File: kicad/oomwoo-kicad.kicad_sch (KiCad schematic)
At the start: 0 parts

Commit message: Battery charging
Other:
- added sheet BATTERY-CHARGER (Battery-Charger.kicad_sch)
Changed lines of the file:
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@@
+	)
+	(sheet
+		(at 44.45 346.71)
+		(size 40.64 25.4)
+		(exclude_from_sim no)
+		(in_bom yes)
+		(on_board yes)
+		(dnp no)
+		(fields_autoplaced yes)
+		(stroke
+			(width 0.1524)
+			(type solid)
+		)
+		(fill
+			(color 0 0 0 0)
+		)
+		(property "Sheetname" "BATTERY-CHARGER"
+			(at 44.45 345.9984 0)
+			(show_name no)
+			(do_not_autoplace no)
+			(effects
+				(font
+					(size 1.27 1.27)
+				)
+				(justify left bottom)
+			)
+		)
+		(property "Sheetfile" "Battery-Charger.kicad_sch"
+			(at 44.45 372.6946 0)
+			(show_name no)
+			(do_not_autoplace no)
+			(effects
+				(font
+					(size 1.27 1.27)
+				)
+				(justify left top)
+			)
+		)
+		(instances
+			(project "oomwoo-kicad"
+				(path "/dbcfb655-8d45-4808-9a74-2a0eb03372e8"
+					(page "34")
+				)
+			)
+		)
 	)
 	(sheet

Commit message: Added Pi CM4/CM5
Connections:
- no-connect marks 4 -> 5
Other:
- removed sheet RK3562
- removed sheet WIFI-BT
- added sheet CM5-GPIO (CM5-GPIO.kicad_sch)
- added sheet CM5-HIGHSPEED (CM5-Highspeed.kicad_sch)
- sheet BATTERY-CHARGER ports: added D+, D-, ID, SCL, SDA, ~{INT}; removed none
- sheet CAMERA ports: added CAM_IO, CM4_CAM0_C_N, CM4_CAM0_C_P, CM4_CAM0_D0_N, CM4_CAM0_D0_P, CM4_CAM0_D1_N, CM4_CAM0_D1_P, ID_SC, ID_SD, MIPI0_C_N, MIPI0_C_P, MIPI0_D0_N, MIPI0_D0_P, MIPI0_D1_N, MIPI0_D1_P, MIPI1_C_N, MIPI1_C_P, MIPI1_D0_N, MIPI1_D0_P, MIPI1_D1_N, MIPI1_D1_P, SCL0, SDA0; removed CAM_CLK0_OUT, CAM_PDN0_L, CAM_RST0_L, I2C4_SCL_M0, I2C4_SDA_M0, MIPI_CSI_RX0_CLK0N, MIPI_CSI_RX0_CLK0P, MIPI_CSI_RX0_D0N, MIPI_CSI_RX0_D0P, MIPI_CSI_RX0_D1N, MIPI_CSI_RX0_D1P, MIPI_CSI_RX0_D2N, MIPI_CSI_RX0_D2P, MIPI_CSI_RX0_D3N, MIPI_CSI_RX0_D3P
- sheet MAIN-FAN ports: added FG, SP; removed MAIN-FAN-S-CTRL, MAIN-FAN-S-SENSE
- sheet MCU-STM32 ports: added BAT_ID, I2C2_SCL, I2C2_SDA, PI-RESET, SUCTION-FAN-FG, SUCTION-FAN-SP, ~{CHG_INT}; removed CHARGE-STATUS, CURENT-SENSE, MAIN-FAN-S-CTRL, MAIN-FAN-S-SENSE, RK-RESET, V-CHARGE-SENSE, VBAT-SENSE
- sheet POWER ports: added none; removed CHARGE-STATUS, CURENT-SENSE, PMIC_EXT_EN, USBC_N, USBC_P, V-CHARGE-SENSE, VBAT-SENSE
- sheet SPEAKER-MIC ports: added BCLK, DIN, DOUT, LRCLK, SP_SHUTDOWN; removed AUDIO-SD, MIC1_IN, MIC2_IN, SPK_N, SPK_P
- note removed: "RK3562"
- note removed: "WF-BT-AP6256"

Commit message: Changed MCU to STM32G473VCT6
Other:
- removed sheet DOCKING-BUMBER
- sheet MAIN-BRUSH MOTOR ports: added MAIN-BRUSH-CURRENT-ADC, MAIN-BRUSH-IN1, MAIN-BRUSH-IN2; removed MAIN-BRUSH, MAIN-BRUSH-F-ADC
- sheet MAIN-FAN ports: added MAIN-FAN-S-CTRL, MAIN-FAN-S-SENSE; removed FG, SP
- sheet MCU-STM32 ports: added I2C3_SCL, I2C3_SDA, MAIN-BRUSH-CURRENT-ADC, MAIN-BRUSH-IN1, MAIN-BRUSH-IN2, MAIN-FAN-S-CTRL, MAIN-FAN-S-SENSE, SIDE-BRUSH-CURRENT-ADC, SIDE-BRUSH-IN1, SIDE-BRUSH-IN2; removed BUMPER-SW1, BUMPER-SW2, DOC-IR-SENS1, DOC-IR-SENS2, I2C2_SCL, I2C2_SDA, MAIN-BRUSH, MAIN-BRUSH-F-ADC, SIDE-BRUSH-L-F-ADC, SIDE-BRUSH-R-F-ADC, SIDE-BRUSH-V-L-CTRL, SIDE-BRUSH-V-R-CTRL, SUCTION-FAN-FG, SUCTION-FAN-SP, WHEEL-M-EN-V
- sheet SIDE-BRUSH ports: added SIDE-BRUSH-CURRENT-ADC, SIDE-BRUSH-IN1, SIDE-BRUSH-IN2; removed SIDE-BRUSH-L-F-ADC, SIDE-BRUSH-R-F-ADC, SIDE-BRUSH-V-L-CTRL, SIDE-BRUSH-V-R-CTRL
- sheet WHEEL MOTOR ports: added none; removed WHEEL-M-EN-V
- note removed: "Controller-RK3562 CONTROLLER TOP"
- note removed: "DOC-IR BUMBER SW"

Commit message: STM32G473VCT6
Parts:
- added R1: 10, symbol Device:R_US
- added R51, R52, R53, R54, R55, R63, R65, R66, R67: 0, symbol Device:R_US
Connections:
- net CM5-GPIO/GPIO07: now also R65.1
- net IMU-CS: now also R53.1
- net IMU-FSYNC: now also R63.1
- net IMU-INT1: now also R55.1
- net IMU-INT2: now also R54.1
- net IMU-MISO: now also R52.1
- net IMU-MOSI: now also R51.1
- net IMU-SCLK: now also R1.1
- new net CM5-GPIO/GPIO22: R63.2
- new net CM5-GPIO/GPIO23: R55.2
- new net CM5-GPIO/GPIO24: R54.2
- new net CM5-GPIO/SPI0_CS0: R53.2
- new net CM5-GPIO/SPI0_MISO: R52.2
- new net CM5-GPIO/SPI0_MOSI: R51.2
- new net CM5-GPIO/SPI0_SCLK: R1.2
- new net CM5-GPIO/UART4_RX: R66.1
- new net CM5-GPIO/UART4_TX: R67.1
- new net LiDAR/LiDAR-MOTOR-CTRL: R65.2
- new net LiDAR/LiDAR-RXD: R67.2
- new net LiDAR/LiDAR-TXD: R66.2
- no-connect marks 5 -> 0
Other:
- added sheet FRONT SENSORS (Front Sensors.kicad_sch)
- added sheet M.2 (M.2.kicad_sch)
- sheet ANTI-FALL ports: added BUMPER_LED_EN, CLIFF_LED_EN; removed none
- sheet CM5-GPIO ports: added SCL1, SDA1, UART4_RX, UART4_TX; removed AUDIO_OUT_L, AUDIO_OUT_R, UART0_RX, UART0_TX
- sheet CM5-HIGHSPEED ports: added PCIE_CLK_N, PCIE_CLK_P, PCIE_CLK_nREQ, PCIE_RX_N, PCIE_RX_P, PCIE_TX_N, PCIE_TX_P, PCIE_nRST, PCIE_nWAKE; removed none
- sheet LiDAR ports: added LiDAR-TXD; removed none
- sheet MCU-STM32 ports: added BUMPER_LED_EN, CLIFF_LED_EN, STM_UART3_RX, STM_UART3_TX, USART4-IR-L-RX, USART4-IR-L-TX, USART4-IR-R-RX, USART4-IR-R-TX, WHEEL-M-LEFT-DROP, WHEEL-M-RIGHT-DROP; removed LiDAR-TXD-HEADER, STM-RESET
- sheet SPEAKER-MIC ports: added none; removed AUDIO-HP-L, AUDIO-HP-R
- sheet WHEEL MOTOR ports: added WHEEL-M-LEFT-DROP, WHEEL-M-RIGHT-DROP; removed none
- note added: "CM5-GPIOS"
- note added: "CM5-HIGHSPEED"
- note added: "FRONT SENSORS"
- note added: "M.2 CONN"

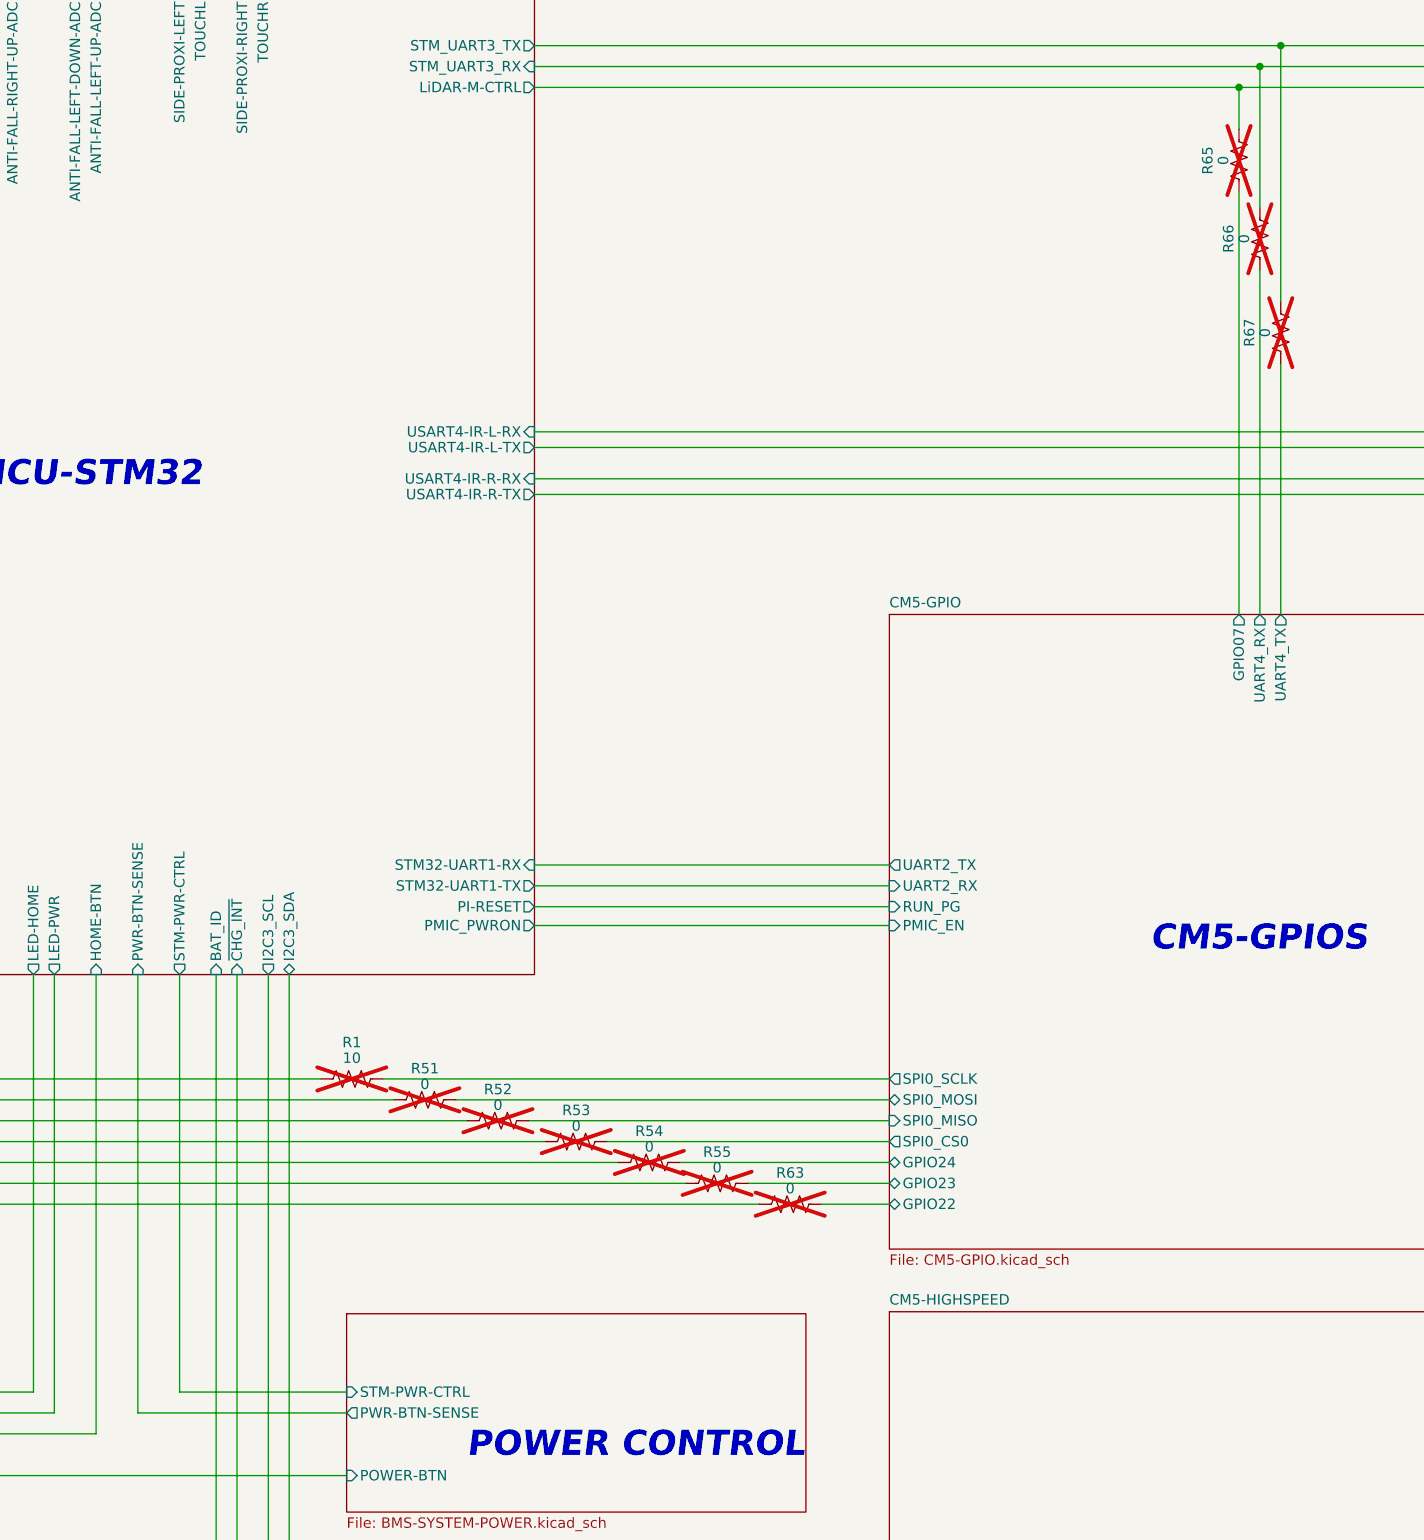
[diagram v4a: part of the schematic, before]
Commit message: RTC clock, signal integrity
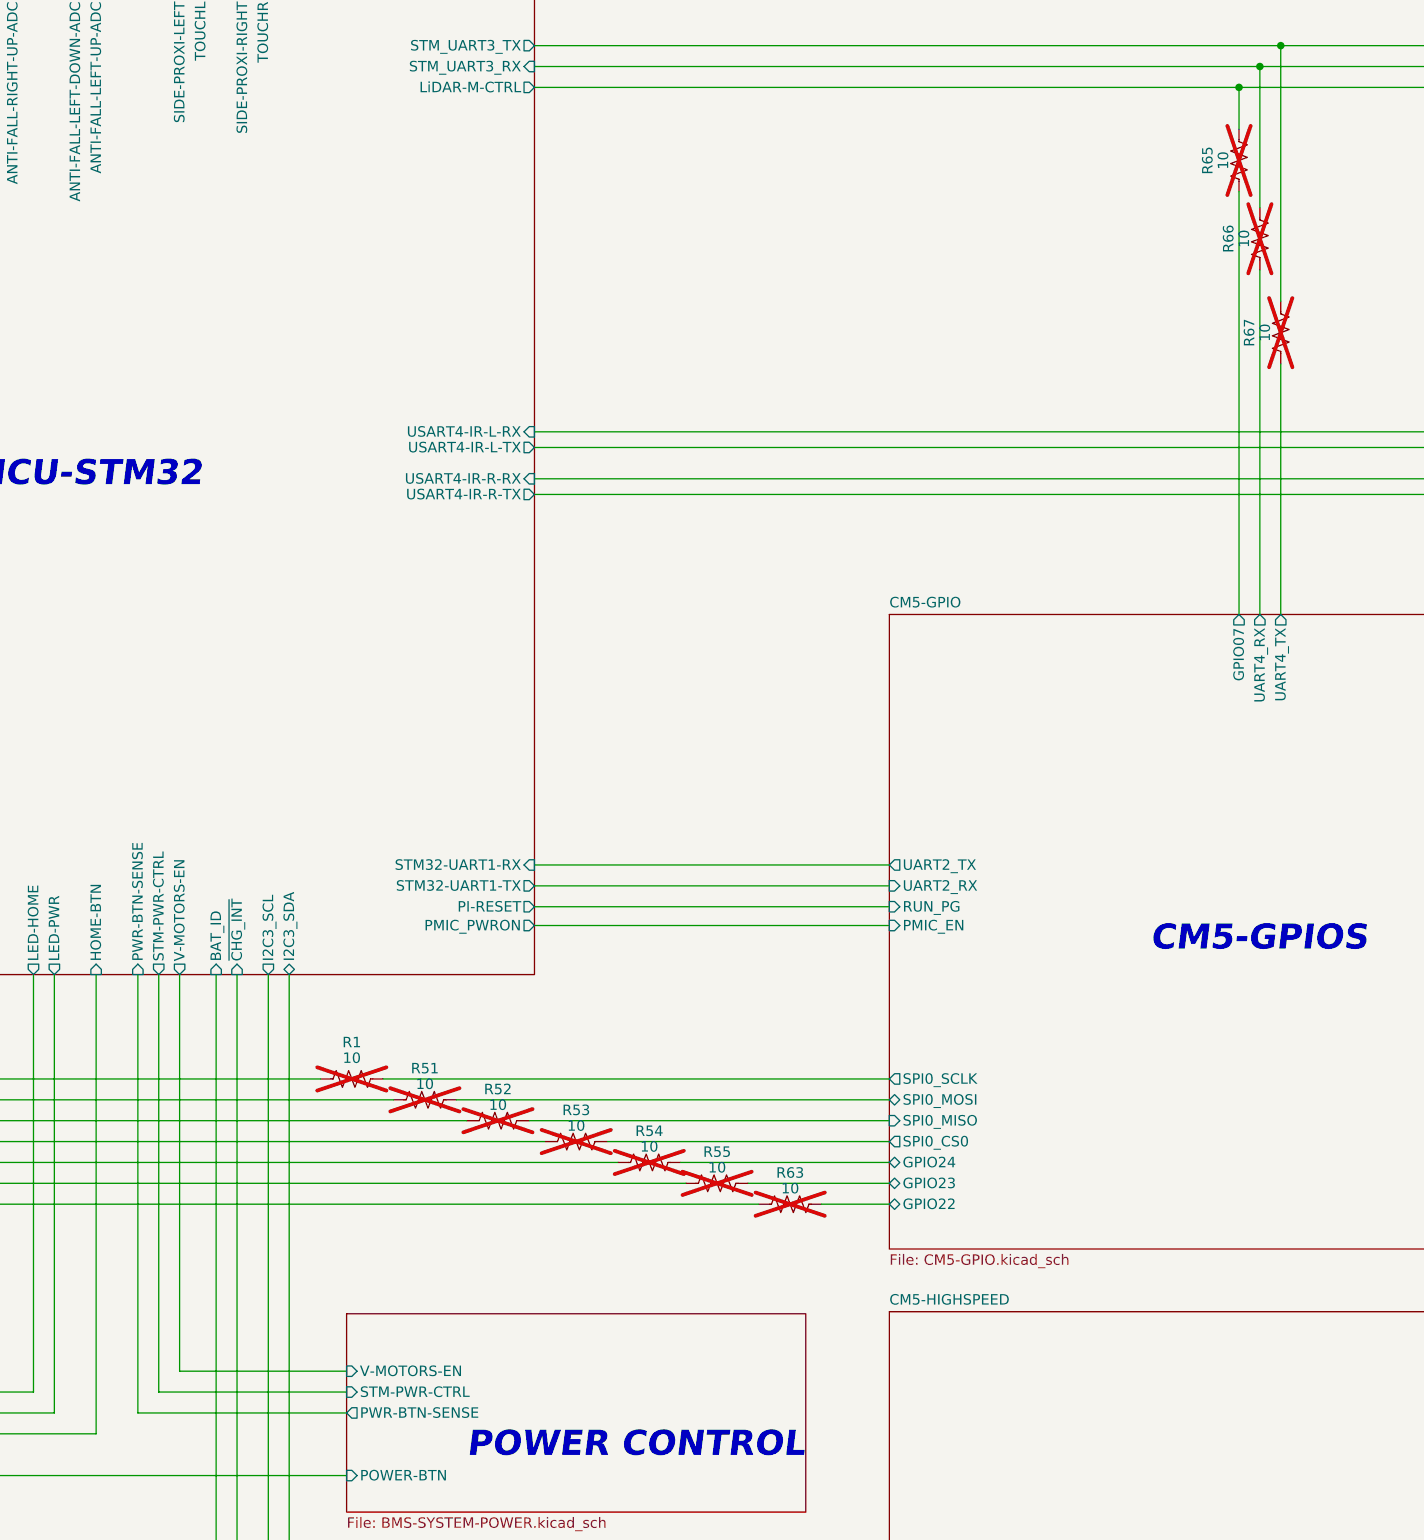
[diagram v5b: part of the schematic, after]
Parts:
- R51, R52, R53, R54, R55, R63, R65, R66, R67: value 0 -> 10
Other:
- sheet MCU-STM32 ports: added V-MOTORS-EN; removed none
- sheet POWER ports: added V-MOTORS-EN; removed none
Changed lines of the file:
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@@
 	(wire
 		(pts
+			(xy 219.71 234.315) (xy 219.71 282.575)
+		)
+		(stroke
+			(width 0)
+			(type default)
+		)
+	)
+	(wire
+		(pts
 			(xy 119.38 116.205) (xy 119.38 133.35)
 		)
@@
 	(wire
 		(pts
+			(xy 219.71 282.575) (xy 240.03 282.575)
+		)
+		(stroke
+			(width 0)
+			(type default)
+		)
+	)
+	(wire
+		(pts
 			(xy 179.07 43.18) (xy 207.01 43.18)
 		)
@@
 	(wire
 		(pts
-			(xy 240.03 285.115) (xy 219.71 285.115)
+			(xy 240.03 285.115) (xy 217.17 285.115)
 		)
 		(stroke
@@
 	(wire
 		(pts
-			(xy 219.71 285.115) (xy 219.71 234.315)
+			(xy 217.17 285.115) (xy 217.17 234.315)
 		)
 		(stroke
@@
 			)
 		)
-		(property "Value" "0"
+		(property "Value" "10"
 			(at 267.97 252.73 90)
 			(show_name no)
@@
 			)
 		)
-		(property "Value" "0"
+		(property "Value" "10"
 			(at 294.005 260.35 90)
 			(show_name no)
@@
 			)
 		)
-		(property "Value" "0"
+		(property "Value" "10"
 			(at 285.115 257.81 90)
 			(show_name no)
@@
 			)
 		)
-		(property "Value" "0"
+		(property "Value" "10"
 			(at 276.86 255.27 90)
 			(show_name no)
@@
 			)
 		)
-		(property "Value" "0"
+		(property "Value" "10"
 			(at 346.71 135.255 90)
 			(show_name no)
@@
 			)
 		)
-		(property "Value" "0"
+		(property "Value" "10"
 			(at 249.555 247.65 90)
 			(show_name no)
@@
 			)
 		)
-		(property "Value" "0"
+		(property "Value" "10"
 			(at 349.25 144.78 90)
 			(show_name no)
@@
 			)
 		)
-		(property "Value" "0"
+		(property "Value" "10"
 			(at 258.445 250.19 90)
 			(show_name no)
@@
 			)
 		)
-		(property "Value" "0"
+		(property "Value" "10"
 			(at 351.79 156.21 90)
 			(show_name no)
@@
 			)
 		)
+		(pin "V-MOTORS-EN" input
+			(at 240.03 282.575 180)
+			(effects
+				(font
+					(size 1.27 1.27)
+				)
+				(justify left)
+			)
+		)
 		(instances
 			(project "oomwoo-kicad"
@@
 		)
 		(pin "STM-PWR-CTRL" output
-			(at 219.71 234.315 270)
+			(at 217.17 234.315 270)
 			(effects
 				(font
@@
 			)
 		)
+		(pin "V-MOTORS-EN" output
+			(at 219.71 234.315 270)
+			(effects
+				(font
+					(size 1.27 1.27)
+				)
+				(justify left)
+			)
+		)

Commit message: External RTC; IR light; side sensors
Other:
- added sheet RTC_WATCHDOG (RTC_WATCHDOG.kicad_sch)
- sheet CM5-GPIO ports: added PMIC_EN2; removed none
- sheet FRONT SENSORS ports: added IR-F-RX1, IR-F-RX2, LIGHT-ON; removed IR-L-RX, IR-L-TX, IR-R-RX, IR-R-TX
- sheet MCU-STM32 ports: added LIGHT-ON, UART3_RX1, UART3_RX2, UART5_RX, UART5_TX, USART2-IR-L-RX, USART2-IR-L-TX; removed SIDE-PROXI-LEFT, SIDE-PROXI-RIGHT, STM_UART3_RX, STM_UART3_TX, TOUCHL, TOUCHR, USART4-IR-L-RX, USART4-IR-L-TX, V-MOTORS-EN
- sheet SIDE-PROXI ports: added IR-L-RX, IR-L-TX, IR-R-RX, IR-R-TX; removed SIDE-PROXI-LEFT, SIDE-PROXI-RIGHT, TOUCHL, TOUCHR
